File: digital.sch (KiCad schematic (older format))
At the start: 4 parts

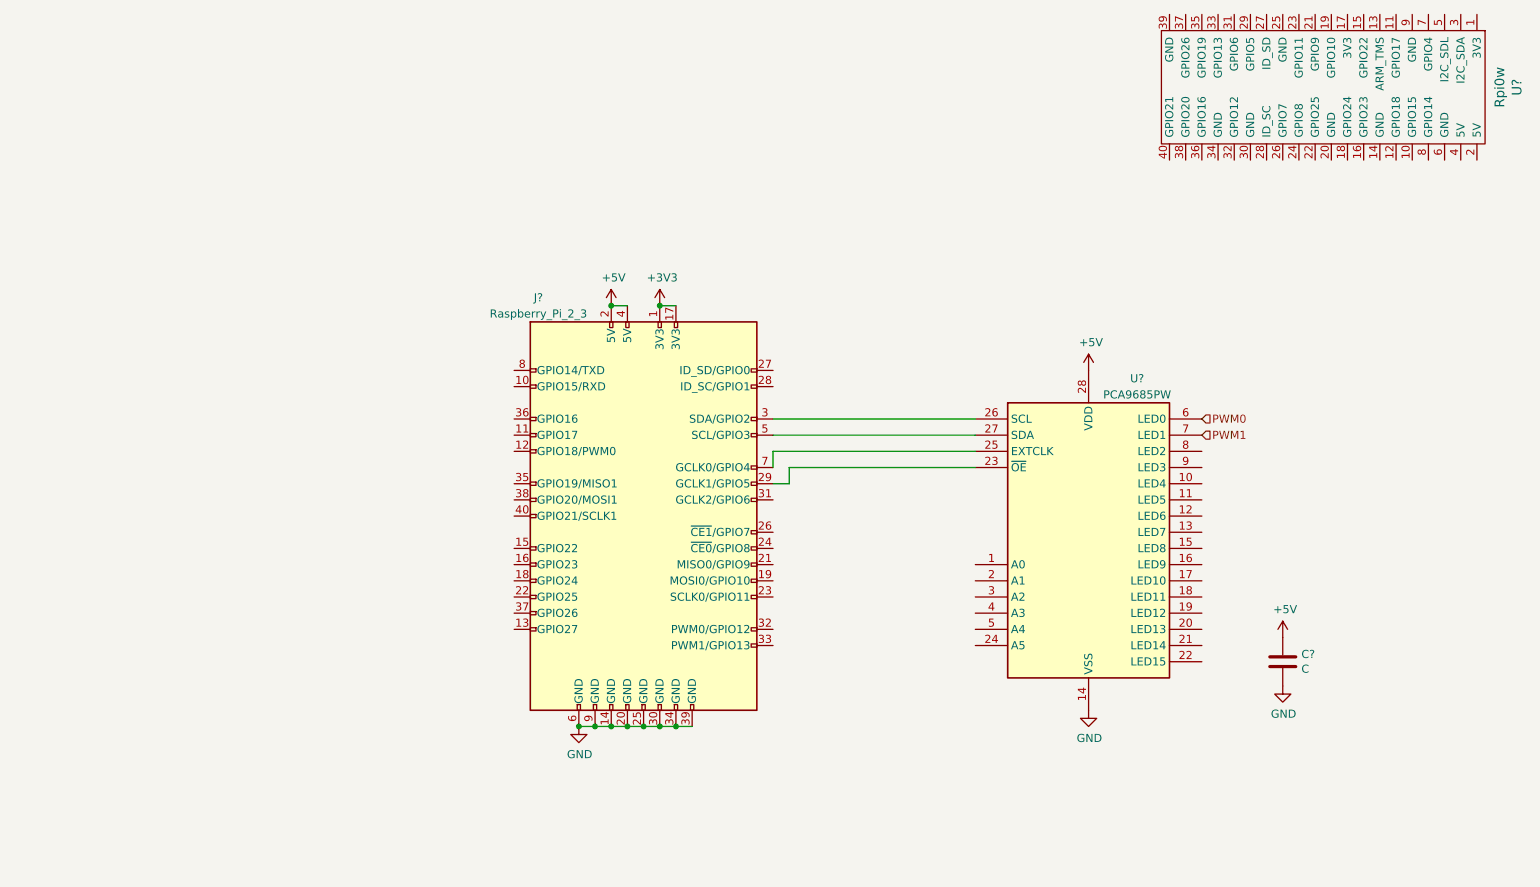
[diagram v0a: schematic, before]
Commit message: Added housekeeping ADC, schematics almost done
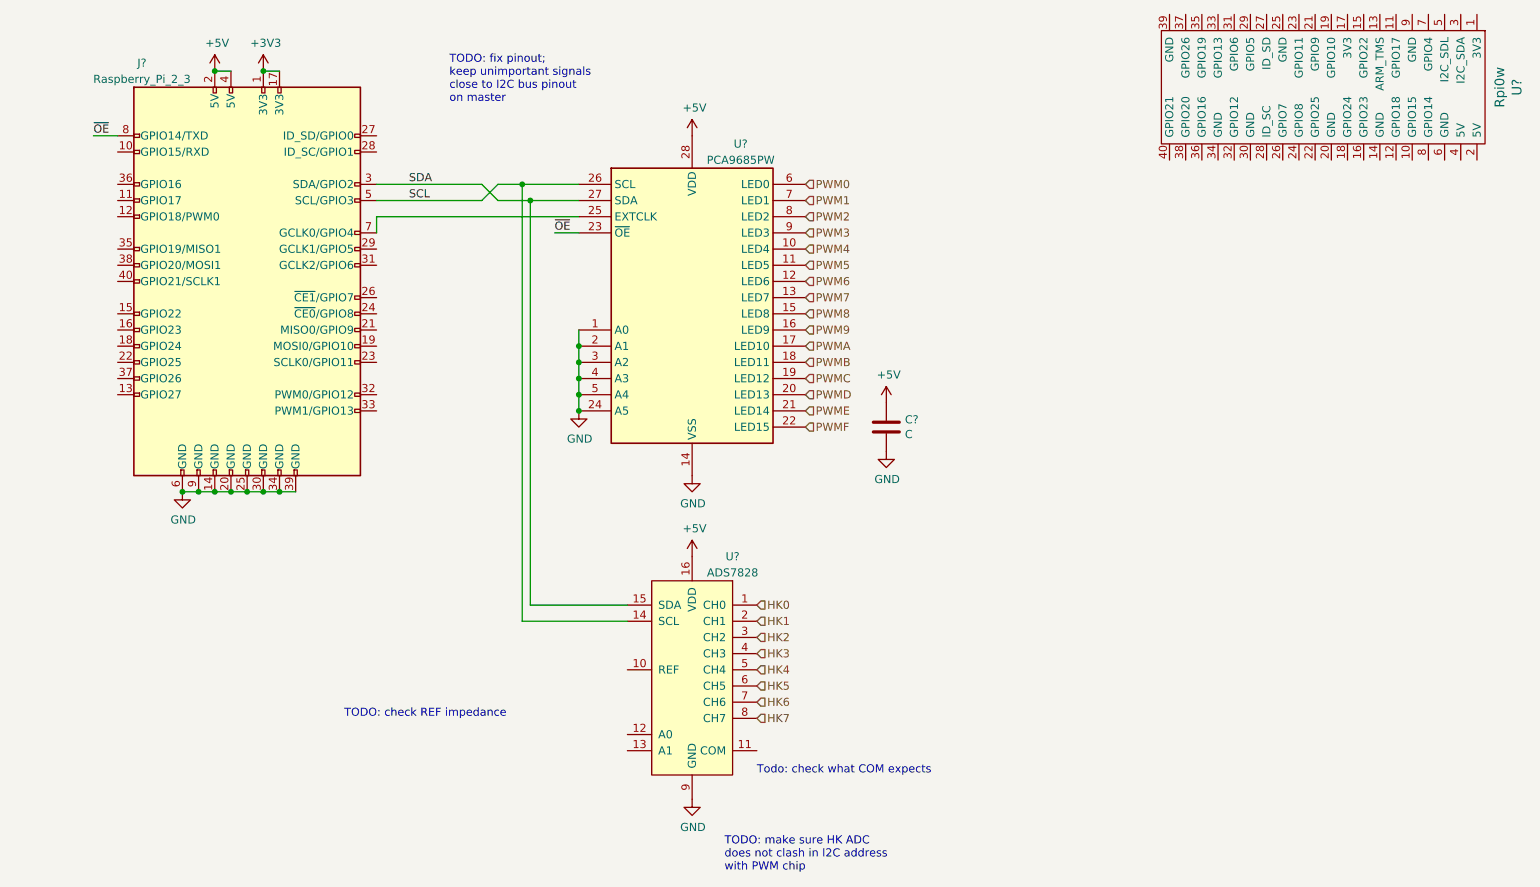
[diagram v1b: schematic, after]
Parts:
- added U?: ADS7828, Package_SO:TSSOP-16_4.4x5mm_P0.65mm, symbol Analog_ADC:ADS7828
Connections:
- net +5V: now also U?.16 (VDD)
- net GND: now also U?.1 (A0), U?.2 (A1), U?.24 (A5), U?.3 (A2), U?.4 (A3), U?.5 (A4), U?.9 (GND)
- net PWM4: now reaches U?.10 (LED4)
- net PWM5: now reaches U?.11 (LED5)
- net PWM6: now reaches U?.12 (LED6)
- net PWM7: now reaches U?.13 (LED7)
- net PWM8: now reaches U?.15 (LED8)
- net PWM9: now reaches U?.16 (LED9)
- net PWMA: now reaches U?.17 (LED10)
- net PWMB: now reaches U?.18 (LED11)
- net PWMC: now reaches U?.19 (LED12)
- net PWMD: now reaches U?.20 (LED13)
- net PWME: now reaches U?.21 (LED14)
- net PWMF: now reaches U?.22 (LED15)
- net at J?.29 (GCLK1/GPIO5): no longer U?.23 (~OE)
- net SCL: now reaches U?.26 (SCL)
- net SCL: now also J?.5 (SCL/GPIO3), U?.14 (SCL); no longer J?.3 (SDA/GPIO2)
- net SDA: now reaches U?.27 (SDA)
- net SDA: now also J?.3 (SDA/GPIO2), U?.15 (SDA); no longer J?.5 (SCL/GPIO3)
- net PWM2: now reaches U?.8 (LED2)
- net PWM3: now reaches U?.9 (LED3)
- net ~OE: now reaches J?.8 (GPIO14/TXD)
- net ~OE: now also U?.23 (~OE)
- new net HK0: U?.1 (CH0)
- new net HK1: U?.2 (CH1)
- new net HK2: U?.3 (CH2)
- new net HK3: U?.4 (CH3)
- new net HK4: U?.5 (CH4)
- new net HK5: U?.6 (CH5)
- new net HK6: U?.7 (CH6)
- new net HK7: U?.8 (CH7)
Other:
- note added: "TODO: check REF impedance\n"
- note added: "TODO: fix pinout;\nkeep unimportant signals\nclose to I2C bus pinout\non master"
- note added: "TODO: make sure HK ADC\ndoes not clash in I2C address\nwith PWM chip"
- note added: "Todo: check what COM expects"
- moved on the sheet: C?, J?, U?

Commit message: Schematics Done. Now need to do footprints
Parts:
- added R1401, R1402, R1403, R1404: R, Resistor_SMD:R_0805_2012Metric, symbol Device:R
- gave numbers to parts that had none: 5
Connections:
- net +3V3: now also U1403.1 (3V3), U1403.17 (3V3)
- net +5V: now also U1403.2 (5V), U1403.4 (5V)
- net GND: now also U1402.11 (COM), U1402.12 (A0), U1402.13 (A1), U1403.14 (GND), U1403.20 (GND), U1403.25 (GND), U1403.30 (GND), U1403.34 (GND), U1403.39 (GND), U1403.6 (GND), U1403.9 (GND), R1401.2, R1402.2
- net HK6: now also R1403.1; no longer U1402.7 (CH6)
- net HK7: now also R1404.2; no longer U1402.8 (CH7)
- net ~FASTCHRG: now reaches J1401.15 (GPIO22)
- net ~FULLCHRG: now reaches J1401.16 (GPIO23)
- net ~FAULT: now reaches J1401.18 (GPIO24)
- net POL4: now reaches J1401.27 (ID_SD/GPIO0)
- net POL5: now reaches J1401.28 (ID_SC/GPIO1)
- net POL0: now reaches J1401.35 (GPIO19/MISO1)
- net POL3: now reaches J1401.36 (GPIO16)
- net POL1: now reaches J1401.38 (GPIO20/MOSI1)
- net POL2: now reaches J1401.40 (GPIO21/SCLK1)
- new net: R1401.1, R1403.2, U1402.7 (CH6)
- new net: R1402.1, R1404.1, U1402.8 (CH7)
- no-connect marks 0 -> 1
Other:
- note added: "2V5 internal ref\n"
- note added: "ADDR BYTE 1000000X\nWhere X = R/~W\n"
- note added: "Addr byte 1001000X\nX specs R/~W"
- note removed: "TODO: check REF impedance\n"
- note removed: "TODO: make sure HK ADC\ndoes not clash in I2C address\nwith PWM chip"
- note removed: "Todo: check what COM expects"
- moved on the sheet: U1403

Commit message: Schematics done, now assigning footprints to do PCB Next
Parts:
- C1401: footprint (none) -> Capacitor_SMD:C_0805_2012Metric
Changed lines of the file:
@@
 F 0 "C1401" H 6915 3446 50  0000 L CNN
 F 1 "C" H 6915 3355 50  0000 L CNN
-F 2 "" H 6838 3250 50  0001 C CNN
+F 2 "Capacitor_SMD:C_0805_2012Metric" H 6838 3250 50  0001 C CNN
 F 3 "~" H 6800 3400 50  0001 C CNN
 	1    6800 3400

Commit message: on to pcbs
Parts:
- J1401: footprint (none) -> Roverschemlib:raspi3
- U1403: footprint (none) -> Roverschemlib:raspi0w
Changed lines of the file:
@@
 F 0 "U1403" H 9150 3897 60  0000 C CNN
 F 1 "Rpi0w" H 9150 3791 60  0000 C CNN
-F 2 "" H 9150 1500 60  0001 C CNN
+F 2 "Roverschemlib:raspi0w" H 9150 1500 60  0001 C CNN
 F 3 "" H 9150 1500 60  0001 C CNN
 	1    9150 1500
@@
 F 0 "J1401" H 2200 3850 50  0000 C CNN
 F 1 "Raspberry_Pi_2_3" H 2200 3750 50  0000 C CNN
-F 2 "" H 2850 2500 50  0001 C CNN
+F 2 "Roverschemlib:raspi3" H 2850 2500 50  0001 C CNN
 F 3 "https://www.raspberrypi.org/documentation/hardware/raspberrypi/schematics/rpi_SCH_3bplus_1p0_reduced.pdf" H 2850 2500 50  0001 C CNN
 	1    2850 2500

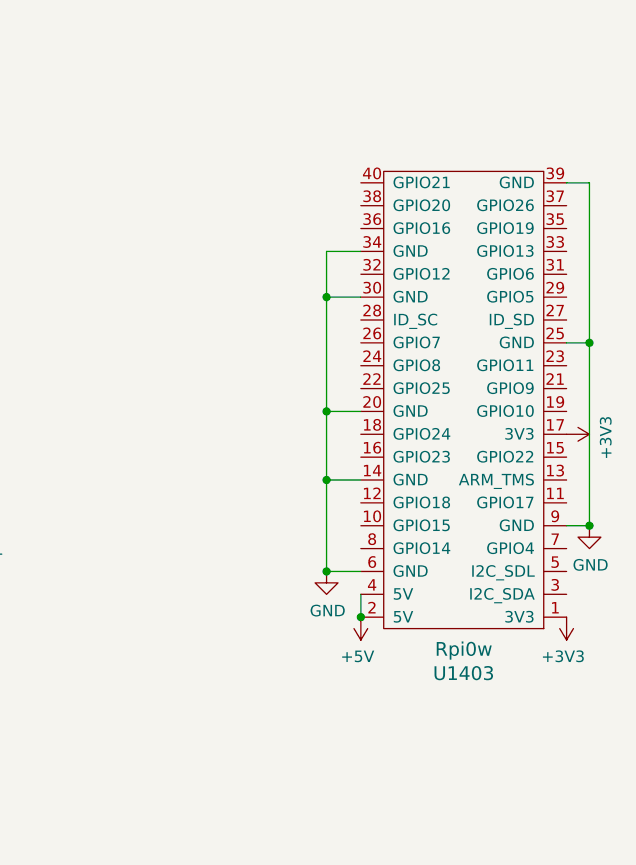
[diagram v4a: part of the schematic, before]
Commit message: updated layout
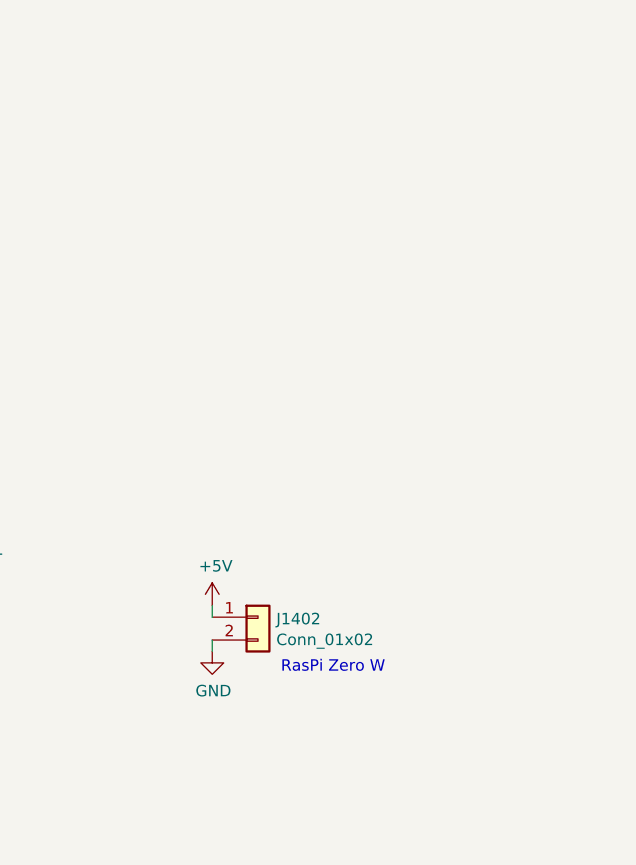
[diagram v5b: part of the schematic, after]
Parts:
- removed U1403: Rpi0w, Roverschemlib:raspi0w, symbol Roverschemlib:Rpi0w
- added J1402: Conn_01x02, Connector_PinSocket_2.54mm:PinSocket_1x02_P2.54mm_Vertical, symbol Connector_Generic:Conn_01x02
- J1401: footprint Roverschemlib:raspi3 -> Connector_PinSocket_2.54mm:PinSocket_2x20_P2.54mm_Vertical
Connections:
- net +5V: now also J1402.1 (Pin_1)
- net GND: now also J1402.2 (Pin_2)
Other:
- note added: "RasPi Zero W"
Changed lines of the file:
@@
 $EndDescr
-$Comp
-L Roverschemlib:Rpi0w U?
-U 1 1 5C4618DA
-P 9150 1500
-AR Path="/5C4618DA" Ref="U?"  Part="1"
-AR Path="/5C46155B/5C4618DA" Ref="U1403"  Part="1"
-F 0 "U1403" H 9150 3897 60  0000 C CNN
-F 1 "Rpi0w" H 9150 3791 60  0000 C CNN
-F 2 "Roverschemlib:raspi0w" H 9150 1500 60  0001 C CNN
-F 3 "" H 9150 1500 60  0001 C CNN
-	1    9150 1500
-	-1   0    0    1
-$EndComp
 $Comp
 L Driver_LED:PCA9685PW U?
@@
 F 0 "J1401" H 2200 3850 50  0000 C CNN
 F 1 "Raspberry_Pi_2_3" H 2200 3750 50  0000 C CNN
-F 2 "Roverschemlib:raspi3" H 2850 2500 50  0001 C CNN
+F 2 "Connector_PinSocket_2.54mm:PinSocket_2x20_P2.54mm_Vertical" H 2850 2500 50  0001 C CNN
 F 3 "https://www.raspberrypi.org/documentation/hardware/raspberrypi/schematics/rpi_SCH_3bplus_1p0_reduced.pdf" H 2850 2500 50  0001 C CNN
 	1    2850 2500
@@
 Text HLabel 3650 1700 2    50   Input ~ 0
 POL5
-$Comp
-L power:+5V #PWR0159
-U 1 1 5C62C327
-P 8700 3650
-F 0 "#PWR0159" H 8700 3500 50  0001 C CNN
-F 1 "+5V" H 8715 3823 50  0000 C CNN
-F 2 "" H 8700 3650 50  0001 C CNN
-F 3 "" H 8700 3650 50  0001 C CNN
-	1    8700 3650
-	-1   0    0    1
-$EndComp
-Wire Wire Line
-	8700 3650 8700 3550
-Connection ~ 8700 3650
-$Comp
-L power:+3V3 #PWR0161
-U 1 1 5C62C6EC
-P 9600 3650
-F 0 "#PWR0161" H 9600 3500 50  0001 C CNN
-F 1 "+3V3" H 9615 3823 50  0000 C CNN
-F 2 "" H 9600 3650 50  0001 C CNN
-F 3 "" H 9600 3650 50  0001 C CNN
-	1    9600 3650
-	-1   0    0    1
-$EndComp
-$Comp
-L power:GND #PWR0220
-U 1 1 5C62C7B7
-P 8550 3450
-F 0 "#PWR0220" H 8550 3200 50  0001 C CNN
-F 1 "GND" H 8555 3277 50  0000 C CNN
-F 2 "" H 8550 3450 50  0001 C CNN
-F 3 "" H 8550 3450 50  0001 C CNN
-	1    8550 3450
-	1    0    0    -1
-$EndComp
-Wire Wire Line
-	8550 3450 8700 3450
-$Comp
-L power:GND #PWR0221
-U 1 1 5C62CB60
-P 9700 3250
-F 0 "#PWR0221" H 9700 3000 50  0001 C CNN
-F 1 "GND" H 9705 3077 50  0000 C CNN
-F 2 "" H 9700 3250 50  0001 C CNN
-F 3 "" H 9700 3250 50  0001 C CNN
-	1    9700 3250
-	1    0    0    -1
-$EndComp
-Wire Wire Line
-	9700 3250 9600 3250
-Wire Wire Line
-	8550 3450 8550 3050
-Wire Wire Line
-	8550 3050 8700 3050
-Connection ~ 8550 3450
-Wire Wire Line
-	8700 2750 8550 2750
-Wire Wire Line
-	8550 2750 8550 3050
-Connection ~ 8550 3050
-Wire Wire Line
-	8700 2250 8550 2250
-Wire Wire Line
-	8550 2250 8550 2750
-Connection ~ 8550 2750
-Wire Wire Line
-	8700 2050 8550 2050
-Wire Wire Line
-	8550 2050 8550 2250
-Connection ~ 8550 2250
-Wire Wire Line
-	9600 1750 9700 1750
-Wire Wire Line
-	9700 1750 9700 2450
-Connection ~ 9700 3250
-Wire Wire Line
-	9600 2450 9700 2450
-Connection ~ 9700 2450
-Wire Wire Line
-	9700 2450 9700 3250
-$Comp
-L power:+3V3 #PWR0222
-U 1 1 5C62EF77
-P 9600 2850
-F 0 "#PWR0222" H 9600 2700 50  0001 C CNN
-F 1 "+3V3" H 9615 3023 50  0000 C CNN
-F 2 "" H 9600 2850 50  0001 C CNN
-F 3 "" H 9600 2850 50  0001 C CNN
-	1    9600 2850
-	0    1    1    0
-$EndComp
 Text HLabel 7300 5100 2    50   Input ~ 0
 HK6
@@
 	6000 5700 5600 5700
 Connection ~ 5600 5700
+$Comp
+L Connector_Generic:Conn_01x02 J1402
+U 1 1 5C823214
+P 8250 3650
+F 0 "J1402" H 8330 3642 50  0000 L CNN
+F 1 "Conn_01x02" H 8330 3551 50  0000 L CNN
+F 2 "Connector_PinSocket_2.54mm:PinSocket_1x02_P2.54mm_Vertical" H 8250 3650 50  0001 C CNN
+F 3 "~" H 8250 3650 50  0001 C CNN
+	1    8250 3650
+	1    0    0    -1
+$EndComp
+$Comp
+L power:+5V #PWR0159
+U 1 1 5C8233E1
+P 8050 3600
+F 0 "#PWR0159" H 8050 3450 50  0001 C CNN
+F 1 "+5V" H 8065 3773 50  0000 C CNN
+F 2 "" H 8050 3600 50  0001 C CNN
+F 3 "" H 8050 3600 50  0001 C CNN
+	1    8050 3600
+	1    0    0    -1
+$EndComp
+Wire Wire Line
+	8050 3600 8050 3650
+$Comp
+L power:GND #PWR0161
+U 1 1 5C823ACE
+P 8050 3800
+F 0 "#PWR0161" H 8050 3550 50  0001 C CNN
+F 1 "GND" H 8055 3627 50  0000 C CNN
+F 2 "" H 8050 3800 50  0001 C CNN
+F 3 "" H 8050 3800 50  0001 C CNN
+	1    8050 3800
+	1    0    0    -1
+$EndComp
+Wire Wire Line
+	8050 3800 8050 3750
+Text Notes 8350 3900 0    50   ~ 0
+RasPi Zero W
 $EndSCHEMATC
